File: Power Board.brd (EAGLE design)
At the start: 64.8 x 91.4 mm, 46 parts, among them Q1 IRLB8743PBF, U2 D24V22F3, U3 D24V22F5, U4 LTC7004, U5 CD4011BPWR, U6 LMR33630ADDA

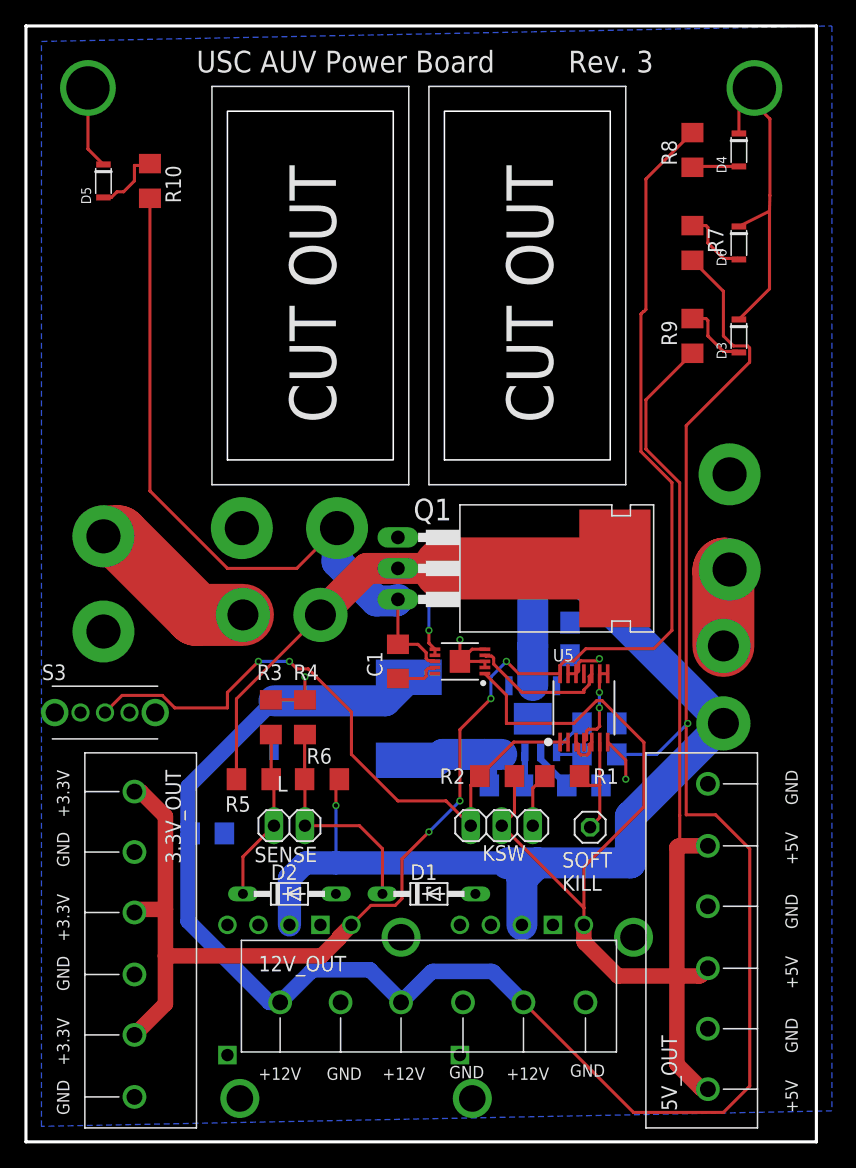
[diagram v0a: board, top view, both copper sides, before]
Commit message: Change 800 ohm resistor to 1K
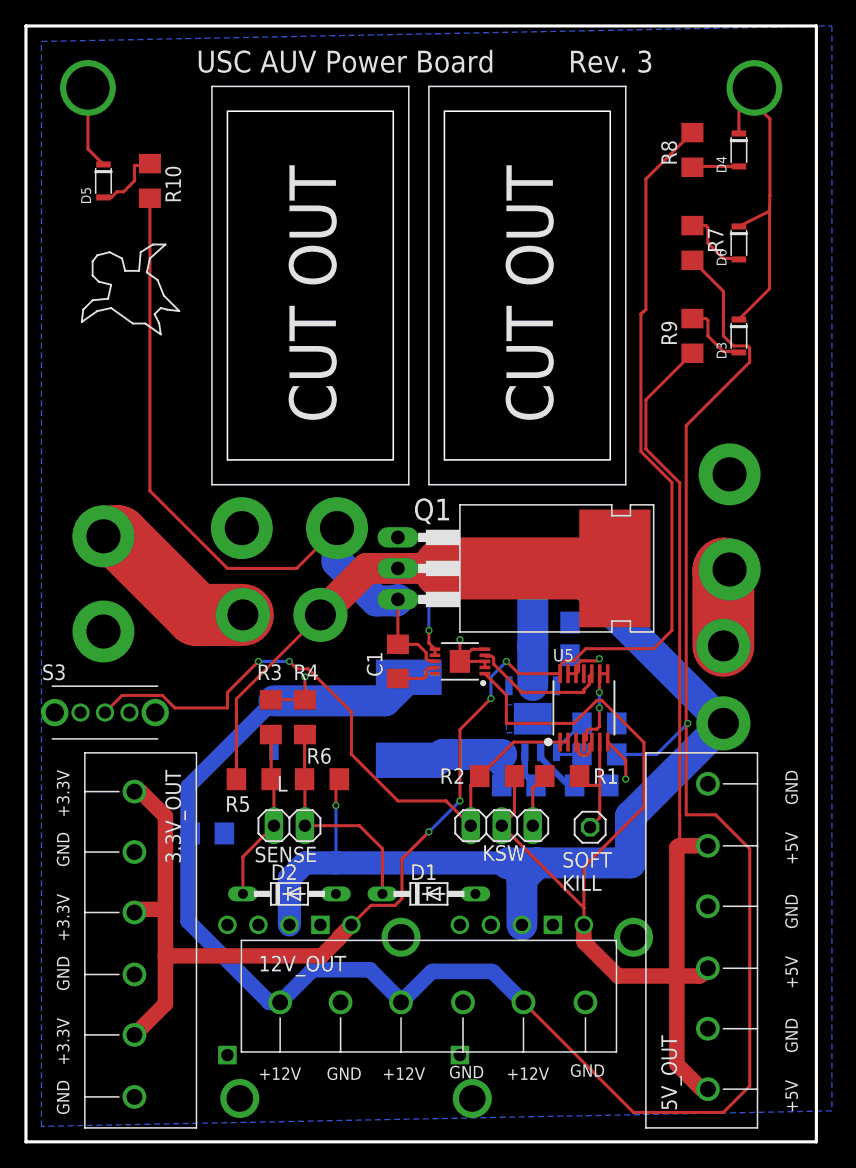
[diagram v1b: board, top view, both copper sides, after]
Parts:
- moved C5 1.02 mm to (23.9, 55.9)
- moved C2 0.63 mm to (29.8, 55.9)
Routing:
- net N$8: track 3.65 -> 4.21 mm
